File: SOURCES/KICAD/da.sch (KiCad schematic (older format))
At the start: 176 parts, among them IC301 IC_OPA1652AIDR, IC302 IC_OPA1652AIDR, IC303 IC_OPA1652AIDR, IC304 IC_OPA1652AIDR, IC305 IC_AK4458VN, IC306 IC_OPA1652AIDR, IC307 IC_OPA1652AIDR, IC308 IC_OPA1652AIDR, IC309 IC_OPA1652AIDR, X301 CONN_02X13

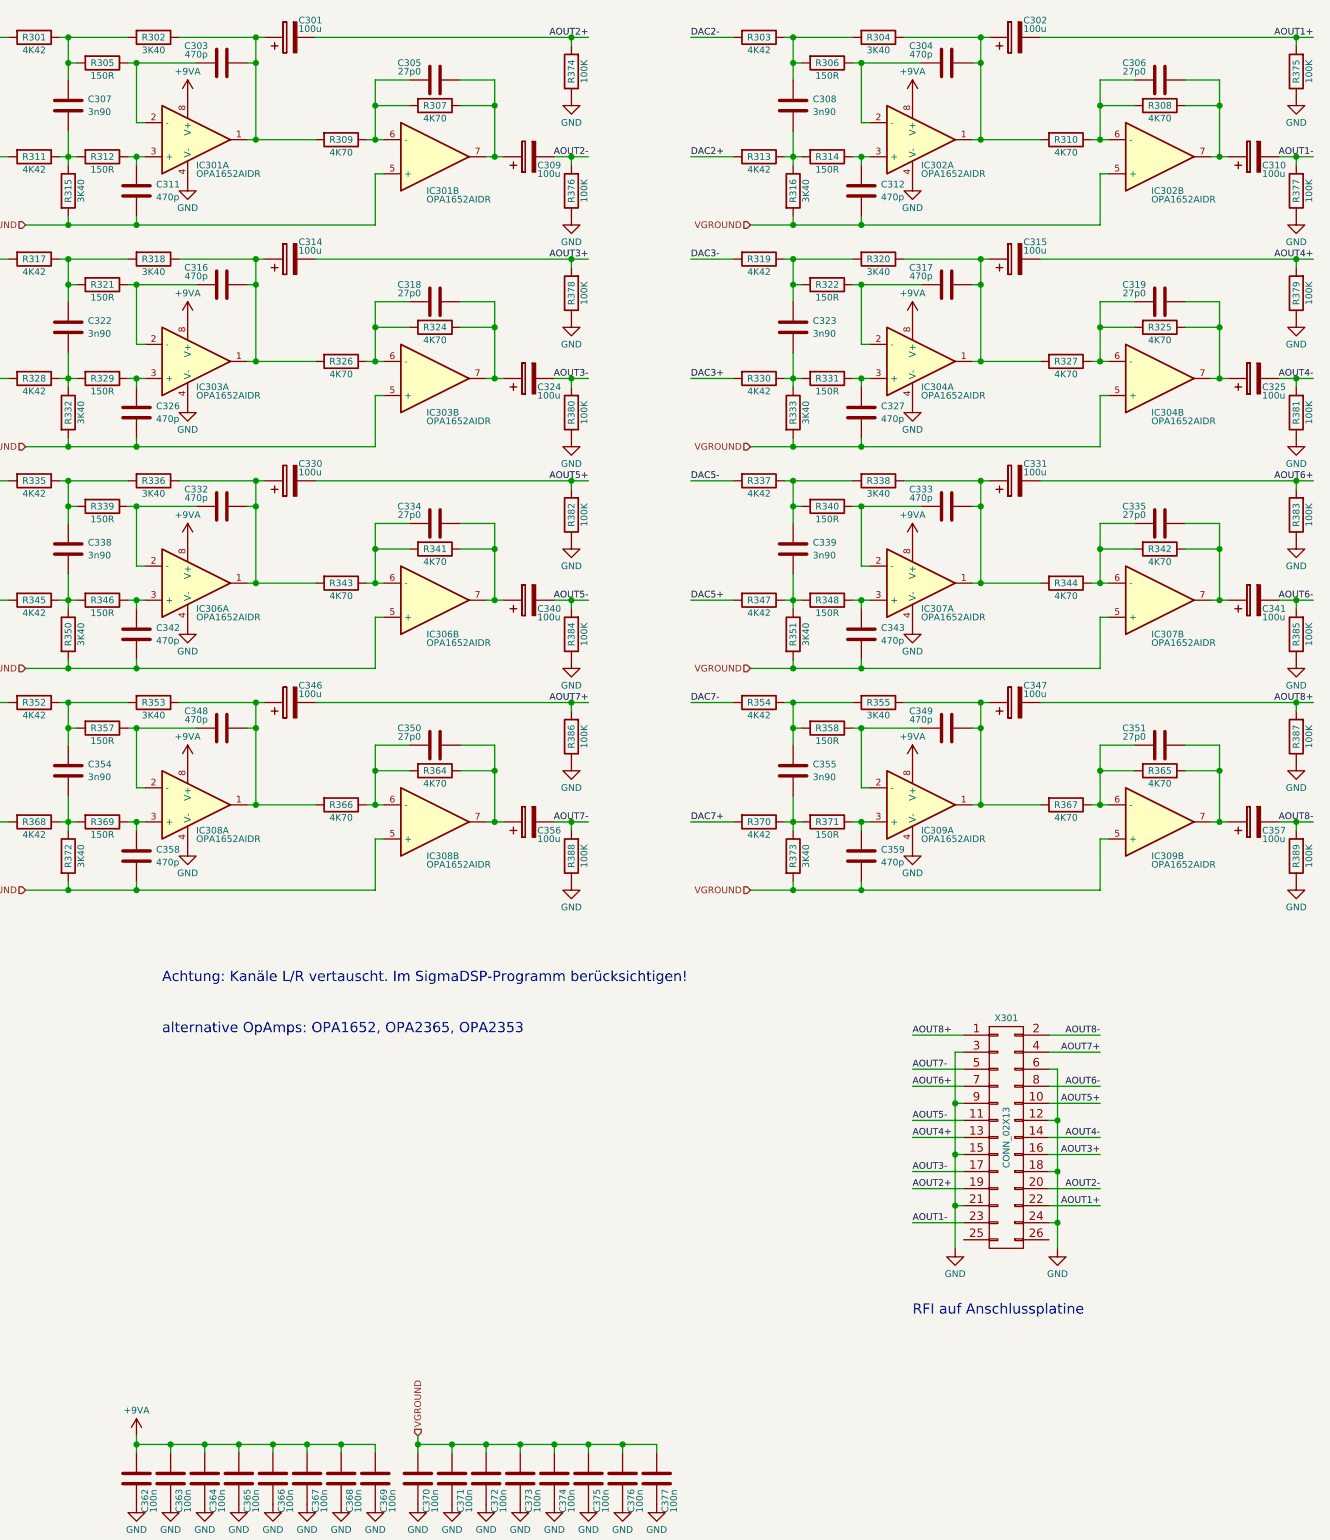
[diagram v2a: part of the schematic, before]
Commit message: Improved ADC input stage
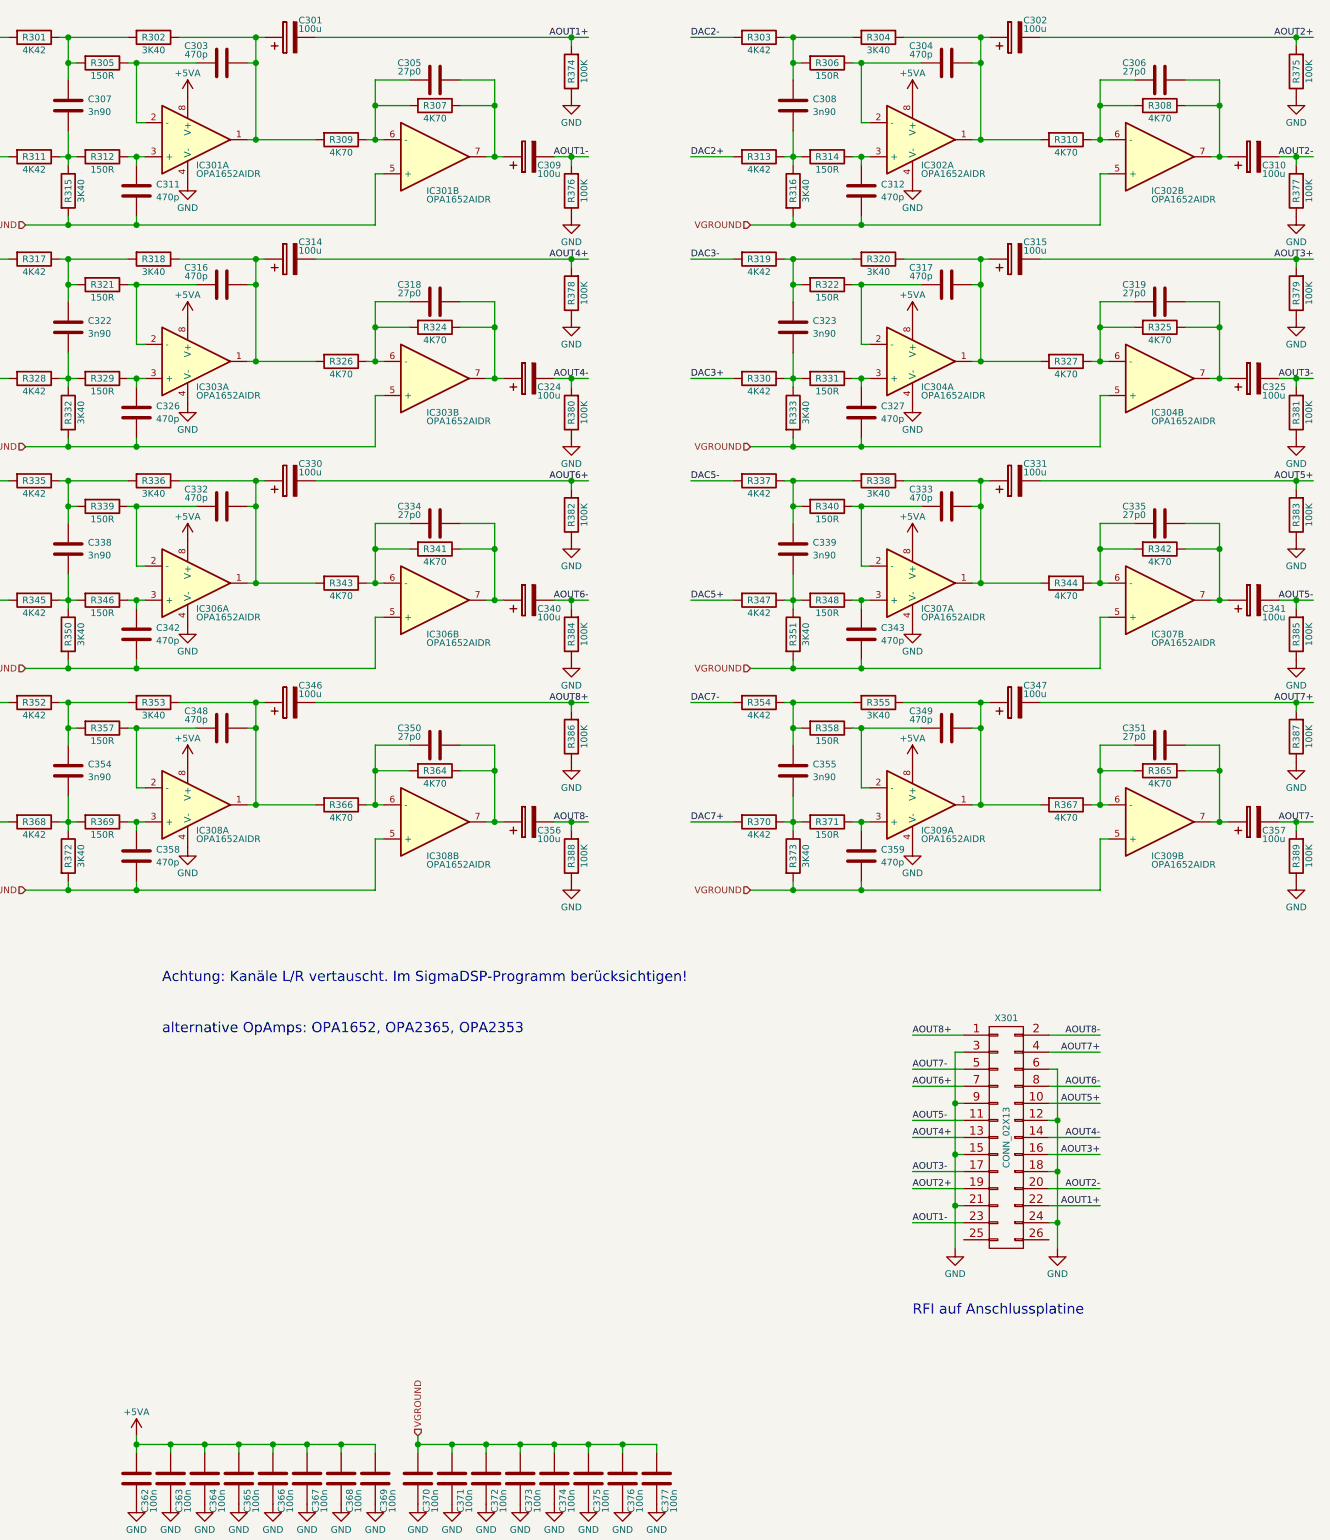
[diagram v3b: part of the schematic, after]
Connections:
- net +9VA is gone; now on net +5VA: C362.1, C363.1, C364.1, C365.1, C366.1, C367.1, C368.1, C369.1, IC301.8 (V+), IC302.8 (V+), IC303.8 (V+), IC304.8 (V+), IC306.8 (V+), IC307.8 (V+), IC308.8 (V+), IC309.8 (V+)
- net AOUT1+: now also C301.2, R374.2; no longer C302.2, R375.2
- net AOUT1-: now also C309.2, R376.2; no longer C310.2, R377.2
- net AOUT2+: now also C302.2, R375.2; no longer C301.2, R374.2
- net AOUT2-: now also C310.2, R377.2; no longer C309.2, R376.2
- net AOUT3+: now also C315.2, R379.2; no longer C314.2, R378.2
- net AOUT3-: now also C325.2, R381.2; no longer C324.2, R380.2
- net AOUT4+: now also C314.2, R378.2; no longer C315.2, R379.2
- net AOUT4-: now also C324.2, R380.2; no longer C325.2, R381.2
- net AOUT5+: now also C331.2, R383.2; no longer C330.2, R382.2
- net AOUT5-: now also C341.2, R385.2; no longer C340.2, R384.2
- net AOUT6+: now also C330.2, R382.2; no longer C331.2, R383.2
- net AOUT6-: now also C340.2, R384.2; no longer C341.2, R385.2
- net AOUT7+: now also C347.2, R387.2; no longer C346.2, R386.2
- net AOUT7-: now also C357.2, R389.2; no longer C356.2, R388.2
- net AOUT8+: now also C346.2, R386.2; no longer C347.2, R387.2
- net AOUT8-: now also C356.2, R388.2; no longer C357.2, R389.2
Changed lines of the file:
@@
 EESchema Schematic File Version 4
 LIBS:freeDSP-aurora-cache
-EELAYER 26 0
+EELAYER 29 0
 EELAYER END
 $Descr A3 16535 11693
@@
 	10950 2900 11050 2900
 Text Label 15400 2900 2    39   ~ 0
-AOUT1-
+AOUT2-
 Text Label 15400 2200 2    39   ~ 0
-AOUT1+
+AOUT2+
 $Comp
 L freeDSP-aurora-rescue:GND #PWR0182
@@
 	10950 4200 11050 4200
 Text Label 11150 4200 2    39   ~ 0
-AOUT3-
+AOUT4-
 Text Label 11150 3500 2    39   ~ 0
-AOUT3+
+AOUT4+
 $Comp
 L freeDSP-aurora-rescue:GND #PWR0183
@@
 	10950 5500 11050 5500
 Text Label 11150 5500 2    39   ~ 0
-AOUT5-
+AOUT6-
 Text Label 11150 4800 2    39   ~ 0
-AOUT5+
+AOUT6+
 $Comp
 L freeDSP-aurora-rescue:GND #PWR0184
@@
 Wire Wire Line
 	10950 6800 11050 6800
-Text Label 11150 6800 2    39   ~ 0
+Text Label 15400 6800 2    39   ~ 0
 AOUT7-
-Text Label 11150 6100 2    39   ~ 0
+Text Label 15400 6100 2    39   ~ 0
 AOUT7+
 $Comp
@@
 	15200 2900 15300 2900
 Text Label 11150 2900 2    39   ~ 0
-AOUT2-
+AOUT1-
 Text Label 11150 2200 2    39   ~ 0
-AOUT2+
+AOUT1+
 $Comp
 L freeDSP-aurora-rescue:GND #PWR0186
@@
 	15200 4200 15300 4200
 Text Label 15400 4200 2    39   ~ 0
-AOUT4-
+AOUT3-
 Text Label 15400 3500 2    39   ~ 0
-AOUT4+
+AOUT3+
 $Comp
 L freeDSP-aurora-rescue:GND #PWR0187
@@
 	15200 5500 15300 5500
 Text Label 15400 5500 2    39   ~ 0
-AOUT6-
+AOUT5-
 Text Label 15400 4800 2    39   ~ 0
-AOUT6+
+AOUT5+
 $Comp
 L freeDSP-aurora-rescue:GND #PWR0188
@@
 Wire Wire Line
 	15200 6800 15300 6800
-Text Label 15400 6800 2    39   ~ 0
+Text Label 11150 6800 2    39   ~ 0
 AOUT8-
-Text Label 15400 6100 2    39   ~ 0
+Text Label 11150 6100 2    39   ~ 0
 AOUT8+
 $Comp
@@
 alternative OpAmps: OPA1652, OPA2365, OPA2353
 $Comp
-L freeDSP-aurora-rescue:+9VA #PWR0191
-U 1 1 5B7AAAFD
-P 8800 2550
-F 0 "#PWR0191" H 8800 2425 50  0001 C CNN
-F 1 "+9VA" H 8800 2700 39  0000 C CNN
-F 2 "" H 8800 2550 50  0001 C CNN
-F 3 "" H 8800 2550 50  0001 C CNN
-	1    8800 2550
-	1    0    0    -1
-$EndComp
-$Comp
-L freeDSP-aurora-rescue:+9VA #PWR0192
-U 1 1 5B7AABA5
-P 13050 2550
-F 0 "#PWR0192" H 13050 2425 50  0001 C CNN
-F 1 "+9VA" H 13050 2700 39  0000 C CNN
-F 2 "" H 13050 2550 50  0001 C CNN
-F 3 "" H 13050 2550 50  0001 C CNN
-	1    13050 2550
-	1    0    0    -1
-$EndComp
-$Comp
-L freeDSP-aurora-rescue:+9VA #PWR0193
-U 1 1 5B7AAC4D
-P 8800 3850
-F 0 "#PWR0193" H 8800 3725 50  0001 C CNN
-F 1 "+9VA" H 8800 4000 39  0000 C CNN
-F 2 "" H 8800 3850 50  0001 C CNN
-F 3 "" H 8800 3850 50  0001 C CNN
-	1    8800 3850
-	1    0    0    -1
-$EndComp
-$Comp
-L freeDSP-aurora-rescue:+9VA #PWR0194
-U 1 1 5B7AACF5
-P 13050 3850
-F 0 "#PWR0194" H 13050 3725 50  0001 C CNN
-F 1 "+9VA" H 13050 4000 39  0000 C CNN
-F 2 "" H 13050 3850 50  0001 C CNN
-F 3 "" H 13050 3850 50  0001 C CNN
-	1    13050 3850
-	1    0    0    -1
-$EndComp
-$Comp
-L freeDSP-aurora-rescue:+9VA #PWR0195
-U 1 1 5B7AAD9D
-P 8800 5150
-F 0 "#PWR0195" H 8800 5025 50  0001 C CNN
-F 1 "+9VA" H 8800 5300 39  0000 C CNN
-F 2 "" H 8800 5150 50  0001 C CNN
-F 3 "" H 8800 5150 50  0001 C CNN
-	1    8800 5150
-	1    0    0    -1
-$EndComp
-$Comp
-L freeDSP-aurora-rescue:+9VA #PWR0196
-U 1 1 5B7AAE45
-P 13050 5150
-F 0 "#PWR0196" H 13050 5025 50  0001 C CNN
-F 1 "+9VA" H 13050 5300 39  0000 C CNN
-F 2 "" H 13050 5150 50  0001 C CNN
-F 3 "" H 13050 5150 50  0001 C CNN
-	1    13050 5150
-	1    0    0    -1
-$EndComp
-$Comp
-L freeDSP-aurora-rescue:+9VA #PWR0197
-U 1 1 5B7AAEED
-P 8800 6450
-F 0 "#PWR0197" H 8800 6325 50  0001 C CNN
-F 1 "+9VA" H 8800 6600 39  0000 C CNN
-F 2 "" H 8800 6450 50  0001 C CNN
-F 3 "" H 8800 6450 50  0001 C CNN
-	1    8800 6450
-	1    0    0    -1
-$EndComp
-$Comp
-L freeDSP-aurora-rescue:+9VA #PWR0198
-U 1 1 5B7AAF95
-P 13050 6450
-F 0 "#PWR0198" H 13050 6325 50  0001 C CNN
-F 1 "+9VA" H 13050 6600 39  0000 C CNN
-F 2 "" H 13050 6450 50  0001 C CNN
-F 3 "" H 13050 6450 50  0001 C CNN
-	1    13050 6450
-	1    0    0    -1
-$EndComp
-$Comp
-L freeDSP-aurora-rescue:+9VA #PWR0199
-U 1 1 5B7ABDFE
-P 8500 10400
-F 0 "#PWR0199" H 8500 10275 50  0001 C CNN
-F 1 "+9VA" H 8500 10550 39  0000 C CNN
-F 2 "" H 8500 10400 50  0001 C CNN
-F 3 "" H 8500 10400 50  0001 C CNN
-	1    8500 10400
-	1    0    0    -1
-$EndComp
-$Comp
 L freeDSP-aurora-rescue:CAP_100u_20%_25V_ALUM_RADIAL C301
 U 1 1 5B7DAFBA
@@
 Text HLabel 10150 10400 1    39   Input ~ 0
 VGROUND
+$Comp
+L freeDSP-aurora-rescue:+5VA #PWR0191
+U 1 1 5C9F5882
+P 8800 2550
+F 0 "#PWR0191" H 8800 2400 50  0001 C CNN
+F 1 "+5VA" H 8800 2690 39  0000 C CNN
+F 2 "" H 8800 2550 50  0000 C CNN
+F 3 "" H 8800 2550 50  0000 C CNN
+	1    8800 2550
+	1    0    0    -1
+$EndComp
+$Comp
+L freeDSP-aurora-rescue:+5VA #PWR0192
+U 1 1 5CA49D89
+P 8800 3850
+F 0 "#PWR0192" H 8800 3700 50  0001 C CNN
+F 1 "+5VA" H 8800 3990 39  0000 C CNN
+F 2 "" H 8800 3850 50  0000 C CNN
+F 3 "" H 8800 3850 50  0000 C CNN
+	1    8800 3850
+	1    0    0    -1
+$EndComp
+$Comp
+L freeDSP-aurora-rescue:+5VA #PWR0193
+U 1 1 5CA9E290
+P 8800 5150
+F 0 "#PWR0193" H 8800 5000 50  0001 C CNN
+F 1 "+5VA" H 8800 5290 39  0000 C CNN
+F 2 "" H 8800 5150 50  0000 C CNN
+F 3 "" H 8800 5150 50  0000 C CNN
+	1    8800 5150
+	1    0    0    -1
+$EndComp
+$Comp
+L freeDSP-aurora-rescue:+5VA #PWR0194
+U 1 1 5CAF325F
+P 8800 6450
+F 0 "#PWR0194" H 8800 6300 50  0001 C CNN
+F 1 "+5VA" H 8800 6590 39  0000 C CNN
+F 2 "" H 8800 6450 50  0000 C CNN
+F 3 "" H 8800 6450 50  0000 C CNN
+	1    8800 6450
+	1    0    0    -1
+$EndComp
+$Comp
+L freeDSP-aurora-rescue:+5VA #PWR0195
+U 1 1 5CB47D26
+P 13050 6450
+F 0 "#PWR0195" H 13050 6300 50  0001 C CNN
+F 1 "+5VA" H 13050 6590 39  0000 C CNN
+F 2 "" H 13050 6450 50  0000 C CNN
+F 3 "" H 13050 6450 50  0000 C CNN
+	1    13050 6450
+	1    0    0    -1
+$EndComp
+$Comp
+L freeDSP-aurora-rescue:+5VA #PWR0196
+U 1 1 5CB9C22D
+P 13050 5150
+F 0 "#PWR0196" H 13050 5000 50  0001 C CNN
+F 1 "+5VA" H 13050 5290 39  0000 C CNN
+F 2 "" H 13050 5150 50  0000 C CNN
+F 3 "" H 13050 5150 50  0000 C CNN
+	1    13050 5150
+	1    0    0    -1
+$EndComp
+$Comp
+L freeDSP-aurora-rescue:+5VA #PWR0197
+U 1 1 5CBF0734
+P 13050 3850
+F 0 "#PWR0197" H 13050 3700 50  0001 C CNN
+F 1 "+5VA" H 13050 3990 39  0000 C CNN
+F 2 "" H 13050 3850 50  0000 C CNN
+F 3 "" H 13050 3850 50  0000 C CNN
+	1    13050 3850
+	1    0    0    -1
+$EndComp
+$Comp
+L freeDSP-aurora-rescue:+5VA #PWR0198
+U 1 1 5CC44C3B
+P 13050 2550
+F 0 "#PWR0198" H 13050 2400 50  0001 C CNN
+F 1 "+5VA" H 13050 2690 39  0000 C CNN
+F 2 "" H 13050 2550 50  0000 C CNN
+F 3 "" H 13050 2550 50  0000 C CNN
+	1    13050 2550
+	1    0    0    -1
+$EndComp
+$Comp
+L freeDSP-aurora-rescue:+5VA #PWR0199
+U 1 1 5CC9AEC2
+P 8500 10400
+F 0 "#PWR0199" H 8500 10250 50  0001 C CNN
+F 1 "+5VA" H 8500 10540 39  0000 C CNN
+F 2 "" H 8500 10400 50  0000 C CNN
+F 3 "" H 8500 10400 50  0000 C CNN
+	1    8500 10400
+	1    0    0    -1
+$EndComp
 $EndSCHEMATC
